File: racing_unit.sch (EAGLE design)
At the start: 65 parts, among them IC2 78M05, IC3 78M05, IC4 78M05, IC5 LM1117-3.3, IC6 78M05, Q1 BDX54C, Q2 BDX54C, Q3 BDX54C, Q4 BDX54C, Q6 BSS138, Q7 BSS138

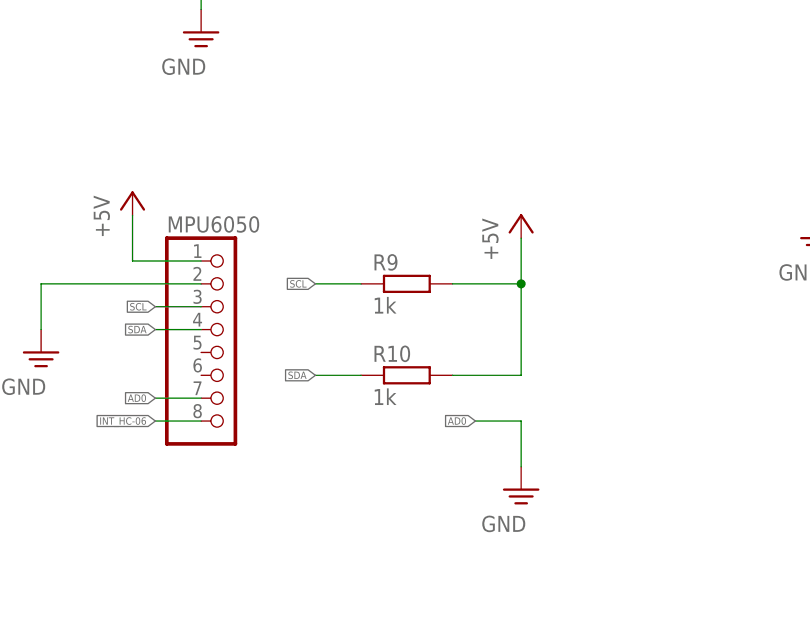
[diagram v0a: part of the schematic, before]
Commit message: changed code to match arduino uno / atmega328p
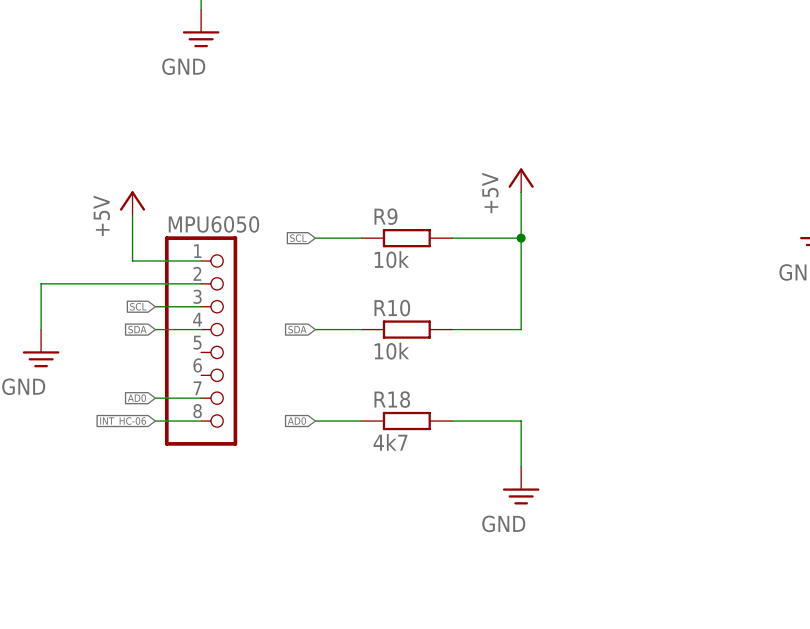
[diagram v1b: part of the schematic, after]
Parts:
- added R18: 4k7, rcl:R-EU_M0805
- R10, R9: value 1k -> 10k
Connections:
- net AD0: now also R18.1
- net GND: now also R18.2
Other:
- moved on the sheet: R10, R9
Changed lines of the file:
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@@
 <part name="R8" library="rcl" deviceset="R-EU_" device="M0805" value="1k"/>
 <part name="R12" library="rcl" deviceset="R-EU_" device="M0805" value="1k"/>
-<part name="R9" library="rcl" deviceset="R-EU_" device="M0805" value="1k"/>
-<part name="R10" library="rcl" deviceset="R-EU_" device="M0805" value="1k"/>
+<part name="R9" library="rcl" deviceset="R-EU_" device="M0805" value="10k"/>
+<part name="R10" library="rcl" deviceset="R-EU_" device="M0805" value="10k"/>
 <part name="R2" library="rcl" deviceset="R-EU_" device="M0805" value="10k"/>
 <part name="R3" library="rcl" deviceset="R-EU_" device="M0805" value="10k"/>
@@
 <part name="SUPPLY22" library="supply2" deviceset="PE" device="" value="GND"/>
 <part name="IC1" library="atmel_tiny24-44-84tiny48-88mega48-88-168-328" deviceset="ATMEGA48/88/168/328" device="-AU"/>
+<part name="R18" library="rcl" deviceset="R-EU_" device="M0805" value="4k7"/>
 </parts>
 <sheets>
@@
 <instance part="SUPPLY17" gate="PE" x="210.82" y="-45.72"/>
 <instance part="GND" gate="PE" x="124.46" y="-58.42"/>
-<instance part="P+12" gate="1" x="177.8" y="-43.18"/>
+<instance part="P+12" gate="1" x="177.8" y="-38.1"/>
 <instance part="GND1" gate="PE" x="177.8" y="-73.66"/>
 <instance part="Q5" gate="G$1" x="83.82" y="-68.58" rot="R90"/>
@@
 <instance part="R8" gate="G$1" x="142.24" y="38.1" rot="R90"/>
 <instance part="R12" gate="G$1" x="162.56" y="38.1" rot="R90"/>
-<instance part="R9" gate="G$1" x="165.1" y="-50.8"/>
-<instance part="R10" gate="G$1" x="165.1" y="-60.96"/>
+<instance part="R9" gate="G$1" x="165.1" y="-45.72"/>
+<instance part="R10" gate="G$1" x="165.1" y="-55.88"/>
 <instance part="R2" gate="G$1" x="248.92" y="-17.78" rot="R90"/>
 <instance part="R3" gate="G$1" x="269.24" y="-17.78" rot="R90"/>
@@
 <instance part="IC1" gate="IC" x="50.8" y="-17.78"/>
 <instance part="IC1" gate="PWR" x="-15.24" y="-7.62"/>
+<instance part="R18" gate="G$1" x="165.1" y="-66.04"/>
 </instances>
 <busses>
@@
 <pinref part="C12" gate="G$1" pin="-"/>
 </segment>
+<segment>
+<pinref part="R18" gate="G$1" pin="2"/>
+<pinref part="GND1" gate="PE" pin="PE"/>
+<wire x1="170.18" y1="-66.04" x2="177.8" y2="-66.04" width="0.1524" layer="91"/>
+<wire x1="177.8" y1="-66.04" x2="177.8" y2="-71.12" width="0.1524" layer="91"/>
+</segment>
 </net>
 <net name="N$9" class="0">
@@
 </segment>
 <segment>
-<wire x1="170.18" y1="-50.8" x2="177.8" y2="-50.8" width="0.1524" layer="91"/>
-<wire x1="177.8" y1="-50.8" x2="177.8" y2="-60.96" width="0.1524" layer="91"/>
-<wire x1="170.18" y1="-60.96" x2="177.8" y2="-60.96" width="0.1524" layer="91"/>
+<wire x1="170.18" y1="-45.72" x2="177.8" y2="-45.72" width="0.1524" layer="91"/>
+<wire x1="177.8" y1="-45.72" x2="177.8" y2="-55.88" width="0.1524" layer="91"/>
+<wire x1="170.18" y1="-55.88" x2="177.8" y2="-55.88" width="0.1524" layer="91"/>
 <pinref part="P+12" gate="1" pin="+5V"/>
-<wire x1="177.8" y1="-50.8" x2="177.8" y2="-45.72" width="0.1524" layer="91"/>
-<junction x="177.8" y="-50.8"/>
+<wire x1="177.8" y1="-45.72" x2="177.8" y2="-40.64" width="0.1524" layer="91"/>
+<junction x="177.8" y="-45.72"/>
 <pinref part="R9" gate="G$1" pin="2"/>
 <pinref part="R10" gate="G$1" pin="2"/>
@@
 </segment>
 <segment>
-<pinref part="GND1" gate="PE" pin="PE"/>
-<wire x1="177.8" y1="-71.12" x2="177.8" y2="-66.04" width="0.1524" layer="91"/>
-<wire x1="177.8" y1="-66.04" x2="172.72" y2="-66.04" width="0.1524" layer="91"/>
-<label x="172.72" y="-66.04" size="0.8128" layer="95" rot="R180" xref="yes"/>
+<wire x1="160.02" y1="-66.04" x2="154.94" y2="-66.04" width="0.1524" layer="91"/>
+<label x="154.94" y="-66.04" size="0.8128" layer="95" rot="R180" xref="yes"/>
+<pinref part="R18" gate="G$1" pin="1"/>
 </segment>
 </net>
@@
 </segment>
 <segment>
-<wire x1="160.02" y1="-50.8" x2="154.94" y2="-50.8" width="0.1524" layer="91"/>
-<label x="154.94" y="-50.8" size="0.8128" layer="95" rot="R180" xref="yes"/>
+<wire x1="160.02" y1="-45.72" x2="154.94" y2="-45.72" width="0.1524" layer="91"/>
+<label x="154.94" y="-45.72" size="0.8128" layer="95" rot="R180" xref="yes"/>
 <pinref part="R9" gate="G$1" pin="1"/>
 </segment>
@@
 </segment>
 <segment>
-<wire x1="160.02" y1="-60.96" x2="154.94" y2="-60.96" width="0.1524" layer="91"/>
-<label x="154.94" y="-60.96" size="0.8128" layer="95" rot="R180" xref="yes"/>
+<wire x1="160.02" y1="-55.88" x2="154.94" y2="-55.88" width="0.1524" layer="91"/>
+<label x="154.94" y="-55.88" size="0.8128" layer="95" rot="R180" xref="yes"/>
 <pinref part="R10" gate="G$1" pin="1"/>
 </segment>

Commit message: improved schematic
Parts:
- removed COIL1, QS-SENSOR: (no value), con-ptr500:AK500/2
- added C22: 10u, rcl:CPOL-EUA/3216-18R
- added L1: 10uH, rcl:L-EU0207/10
- added X1: COIL1, con-ptr500:AK500/2
- added X5: QS-SENSOR, con-ptr500:AK500/2
- C1, C13, C6: value 330n -> 100n
- C10: value 4700uF/25V -> 22p; device rcl:CPOL-EUE7.5-16 -> rcl:C-EUC0805
- C11, C12: value 10u -> 100n; device rcl:CPOL-EUA/3216-18R -> rcl:C-EUC0805
- C14, C17: value 100n -> 330n
- C19, C20: value 100n -> 4700uF/25V; device rcl:C-EUC0805 -> rcl:CPOL-EUE7.5-16
- C21: value 100n -> 10u; device rcl:C-EUC0805 -> rcl:CPOL-EUA/3216-18R
- C8: value 4700uF/25V -> 330n; device rcl:CPOL-EUE7.5-16 -> rcl:C-EUC0805
- C9: value 22p -> 100n
- D1, D2, D3, D4: value 1N4937 -> US1M; device diode:1N4004 -> diode:DIODE-DO214AC
- IC1: value (none) -> 78M05; device atmel_tiny24-44-84tiny48-88mega48-88-168-328:ATMEGA48/88/168/328-AU -> v-reg-2:LM1117TO252
- IC2: value 78M05 -> ATMega328P-AU; device v-reg-2:LM1117TO252 -> atmel_tiny24-44-84tiny48-88mega48-88-168-328:ATMEGA48/88/168/328-AU
- IC5: value LM1117-3.3 -> 78M05; device v-reg-2:LM1117 -> v-reg-2:LM1117TO252
- IC6: value 78M05 -> LM1117-3.3; device v-reg-2:LM1117TO252 -> v-reg-2:LM1117
- JP2: value (none) -> MPU6050
- JP3: value (none) -> HC-06
- JP4: value (none) -> PWR-LED
- Q3: value BDX54C -> 16MHz; device transistor-power:MJE2955 -> crystal:CRYSTALHC49S
- Q5: value (none) -> BDX54C; device crystal:CRYSTALHC49S -> transistor-power:MJE2955
- R1, R12, R17: value 1k -> 10k
- R10, R2, R3: value 10k -> 1k
- R11: value 330R -> 10k; device resistor:R-EU_0204/5 -> rcl:R-EU_M0805
- R13: value 10k -> 4k7
- R18: value 4k7 -> 10k
- R9: value 10k -> 330R; device rcl:R-EU_M0805 -> resistor:R-EU_0204/5
- X2: value (none) -> COIL2
- X3: value (none) -> COIL3
- X4: value (none) -> COIL4
- X6: value (none) -> SUPPLY
- renumbered COIL2 to X2, COIL3 to X3, COIL4 to X4, HC-06 to JP3, MPU6050 to JP2, SUPPLY to X6
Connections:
- removed net PE: C15.2, C18.2, C19.2, C20.2, C21.2
- new net N$5: C9.1, IC2IC.AREF
- new net N$6: C12.1, IC2IC.AVCC, L1.2
- net +3V3: now also C22.+, IC6.OUT, R15.2, R16.2; no longer C12.+, IC5.OUT, R13.2, R2.2
- net +5V: now also C1.1, C19.+, C2.1, C20.+, C21.+, IC2PWR.UCC, IC6.IN, L1.1, R1.1, R11.2, R12.2, R17.2, R18.2, X5-1.KL; no longer C10.+, C11.+, C15.1, C16.1, C17.1, C8.+, IC1IC.AREF, IC1IC.AVCC, IC1PWR.UCC, IC5.IN, QS-SENSOR-1.KL, R10.2, R15.2, R16.1, R3.2, R9.2
- net AD0: now also R13.1; no longer R18.1
- net COIL1-IN: now also C3.1, IC2IC.PD4(T0/XCK/PCINT20), R3.1; no longer C18.1, IC1IC.PD4(T0/XCK/PCINT20), R1.1
- net COIL1-OUT: now also IC2IC.PB0(ICP1/CLKO/PCINT0), R2.2; no longer IC1IC.PB0(ICP1/CLKO/PCINT0), R17.2
- net COIL2-IN: now also C6.1, IC2IC.PD5(T1/OC0B/PCINT21); no longer C19.1, IC1IC.PD5(T1/OC0B/PCINT21)
- net COIL2-OUT: now also IC2IC.PB1(OC1A/PCINT1); no longer IC1IC.PB1(OC1A/PCINT1)
- net COIL3-IN: now also C13.1, IC2IC.PD6(AIN0/OC0A/PCINT22); no longer C20.1, IC1IC.PD6(AIN0/OC0A/PCINT22)
- net COIL3-OUT: now also IC2IC.PB2(SS/OC1B/PCINT2), Q4.B; no longer IC1IC.PB2(SS/OC1B/PCINT2), Q3.B
- net COIL4-IN: now also C16.1, IC2IC.PD7(AIN1/PCINT23), R10.1; no longer C21.1, IC1IC.PD7(AIN1/PCINT23), R12.1
- net GND: now also C10.2, C11.2, C12.2, C15.2, C18.2, C19.-, C20.-, C21.-, C22.-, C7.2, C8.2, C9.2, IC1.GND, IC2PWR.GND, R13.2, R2.1, R9.2; no longer C10.-, C11.-, C12.-, C7.1, C8.-, C9.1, IC1PWR.GND, IC2.GND, R11.2, R17.1, R18.2
- net INT_HC-06: now also IC2IC.PD2(INT0/PCINT18); no longer IC1IC.PD2(INT0/PCINT18)
- net MISO: now also IC2IC.PB4(MISO/PCINT4); no longer IC1IC.PB4(MISO/PCINT4)
- net MOSI/COIL4-OUT: now also IC2IC.PB3(MOSI/OC2A/PCINT3), Q5.B; no longer IC1IC.PB3(MOSI/OC2A/PCINT3), Q4.B
- net N$1: now also C4.1, IC1.IN, X1-1.KL; no longer C6.1, COIL1-1.KL, IC6.IN
- net N$10: now also Q4.C; no longer Q3.C
- net N$12: now also X1-2.KL; no longer COIL1-2.KL
- net N$14: now also IC1.OUT, R3.2; no longer IC6.OUT, R1.2
- net N$15: now also C11.1, IC3.OUT; no longer C3.1, IC2.OUT
- net N$17: now also C18.1, IC5.OUT, R10.2; no longer C14.1, IC4.OUT, R12.2
- net N$2: now also C8.1, IC3.IN; no longer C4.1, IC2.IN
- net N$21: now also C15.1, IC4.OUT; no longer C2.1, IC3.OUT
- net N$3: now also C14.1, IC4.IN, Q4.E; no longer C1.1, IC3.IN, Q3.E
- net N$4: now also C17.1, IC5.IN, Q5.E; no longer C13.1, IC4.IN, Q4.E
- net N$9: now also Q5.C; no longer Q4.C
- net QS-SENSOR: now also IC2IC.PC0(ADC0/PCINT8), R9.1, X5-2.KL; no longer IC1IC.PC0(ADC0/PCINT8), QS-SENSOR-2.KL, R11.1
- net RESET: now also IC2IC.PC6(!RESET!/PCINT14), R1.2; no longer IC1IC.PC6(!RESET!/PCINT14), R16.2
- net RX_ATMEGA: now also IC2IC.PD0(RXD/PCINT16), R17.1; no longer IC1IC.PD0(RXD/PCINT16), R3.1
- net RX_HC-06: now also R16.1; no longer R13.1
- net SCK: now also IC2IC.PB5(SCK/PCINT5); no longer IC1IC.PB5(SCK/PCINT5)
- net SCL: now also IC2IC.PC5(ADC5/SCL/PCINT13), R11.1; no longer IC1IC.PC5(ADC5/SCL/PCINT13), R9.1
- net SDA: now also IC2IC.PC4(ADC4/SDA/PCINT12), R12.1; no longer IC1IC.PC4(ADC4/SDA/PCINT12), R10.1
- net TX_ATMEGA: now also IC2IC.PD1(TXD/PCINT17), R18.1; no longer IC1IC.PD1(TXD/PCINT17), R15.1
- net TX_HC-06: now also R15.1; no longer R2.1
- net XTAL1: now also C7.1, IC2IC.PB6(XTAL1/TOSC1/PCINT6), Q3.2; no longer C7.2, IC1IC.PB6(XTAL1/TOSC1/PCINT6), Q5.2
- net XTAL2: now also C10.1, IC2IC.PB7(XTAL2/TOSC2/PCINT7), Q3.1; no longer C9.2, IC1IC.PB7(XTAL2/TOSC2/PCINT7), Q5.1
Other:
- moved on the sheet: C1, C13, C14, C15, C16, C17, C18, C2, C3, C4, C6, C7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
